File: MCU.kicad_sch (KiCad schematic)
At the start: 23 parts, among them J1 Conn_ARM_SWD_TagConnect_TC203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, U1 MCU_0001, Y1 CLK_0001, Y2 CLK_0002

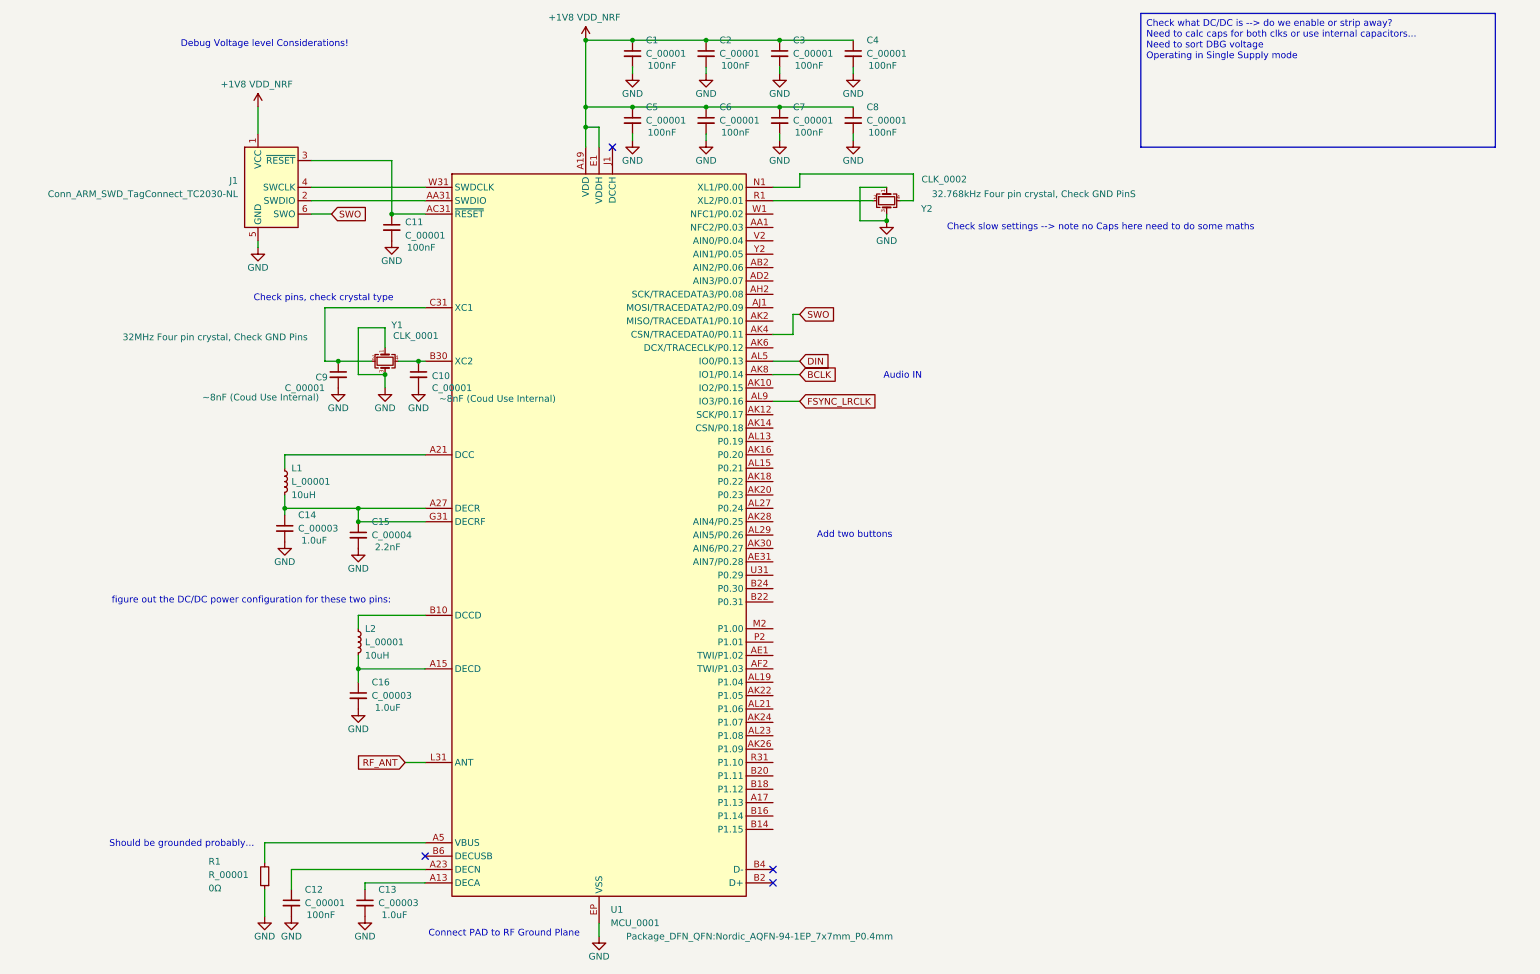
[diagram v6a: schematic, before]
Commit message: added NORA-B106 module, routed SWD/SWO, + power + audio
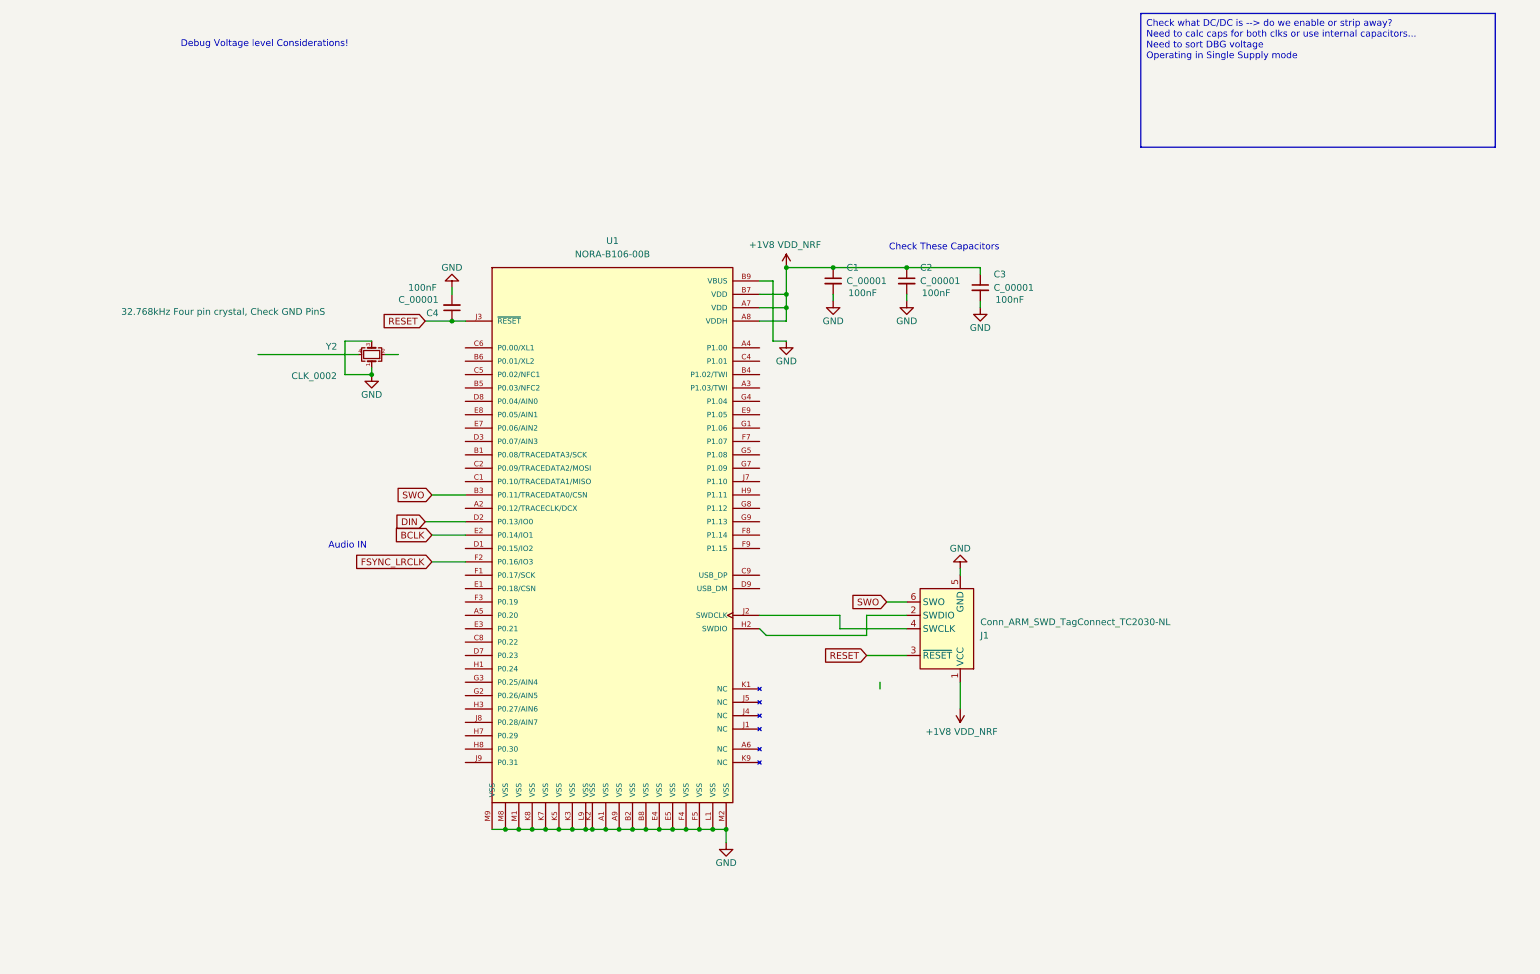
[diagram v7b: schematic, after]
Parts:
- removed C10, C9: C_00001, symbol mic_patch_parts:C_00002
- removed C11, C12, C5, C6, C7, C8: C_00001, symbol mic_patch_parts:C_00001
- removed C13, C14, C16: C_00003, symbol mic_patch_parts:C_00003
- removed C15: C_00004, symbol mic_patch_parts:C_00004
- removed L1, L2: L_00001, symbol mic_patch_parts:L_00001
- removed R1: R_00001, symbol mic_patch_parts:R_00001
- removed U1: MCU_0001, Package_DFN_QFN:Nordic_AQFN-94-1EP_7x7mm_P0.4mm, symbol mic_patch_parts:MCU_0001
- removed Y1: CLK_0001, symbol mic_patch_parts:CLK_0001
- added U1: NORA-B106-00B, NORA-B106-00B:XCVR_NORA-B106-00B, symbol mic_patch_parts:NORA-B106-00B
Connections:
- net +1V8 VDD_NRF: now also U1.A7 (VDD), U1.A8 (VDDH), U1.B7 (VDD); no longer C4.1
- net BCLK: now also U1.E2 (P0.14/IO1)
- net DIN: now also U1.D2 (P0.13/IO0)
- net FSYNC_LRCLK: now also U1.F2 (P0.16/IO3)
- net GND: now also U1.A1 (VSS), U1.A9 (VSS), U1.B2 (VSS), U1.B8 (VSS), U1.B9 (VBUS), U1.E4 (VSS), U1.E5 (VSS), U1.F4 (VSS), U1.F5 (VSS), U1.K2 (VSS), U1.K3 (VSS), U1.K5 (VSS), U1.K7 (VSS), U1.K8 (VSS), U1.L1 (VSS), U1.L9 (VSS), U1.M1 (VSS), U1.M2 (VSS), U1.M8 (VSS), U1.M9 (VSS)
- net SWO: now also U1.B3 (P0.11/TRACEDATA0/CSN)
- net at J1.2 (SWDIO): now also U1.H2 (SWDIO)
- net RESET: now reaches J1.3 (~{RESET})
- net RESET: now also C4.1, U1.J3 (~{RESET})
- net at J1.4 (SWCLK): now also U1.J2 (SWDCLK)
- no-connect marks 4 -> 0
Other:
- note added: "Check These Capacitors"
- note removed: "Add two buttons"
- note removed: "Check pins, check crystal type"
- note removed: "Check slow settings --> note no Caps here need to do some maths"
- note removed: "Connect PAD to RF Ground Plane"
- note removed: "Should be grounded probably..."
- note removed: "figure out the DC/DC power configuration for these two pins:"
- moved on the sheet: C1, C2, J1, Y2

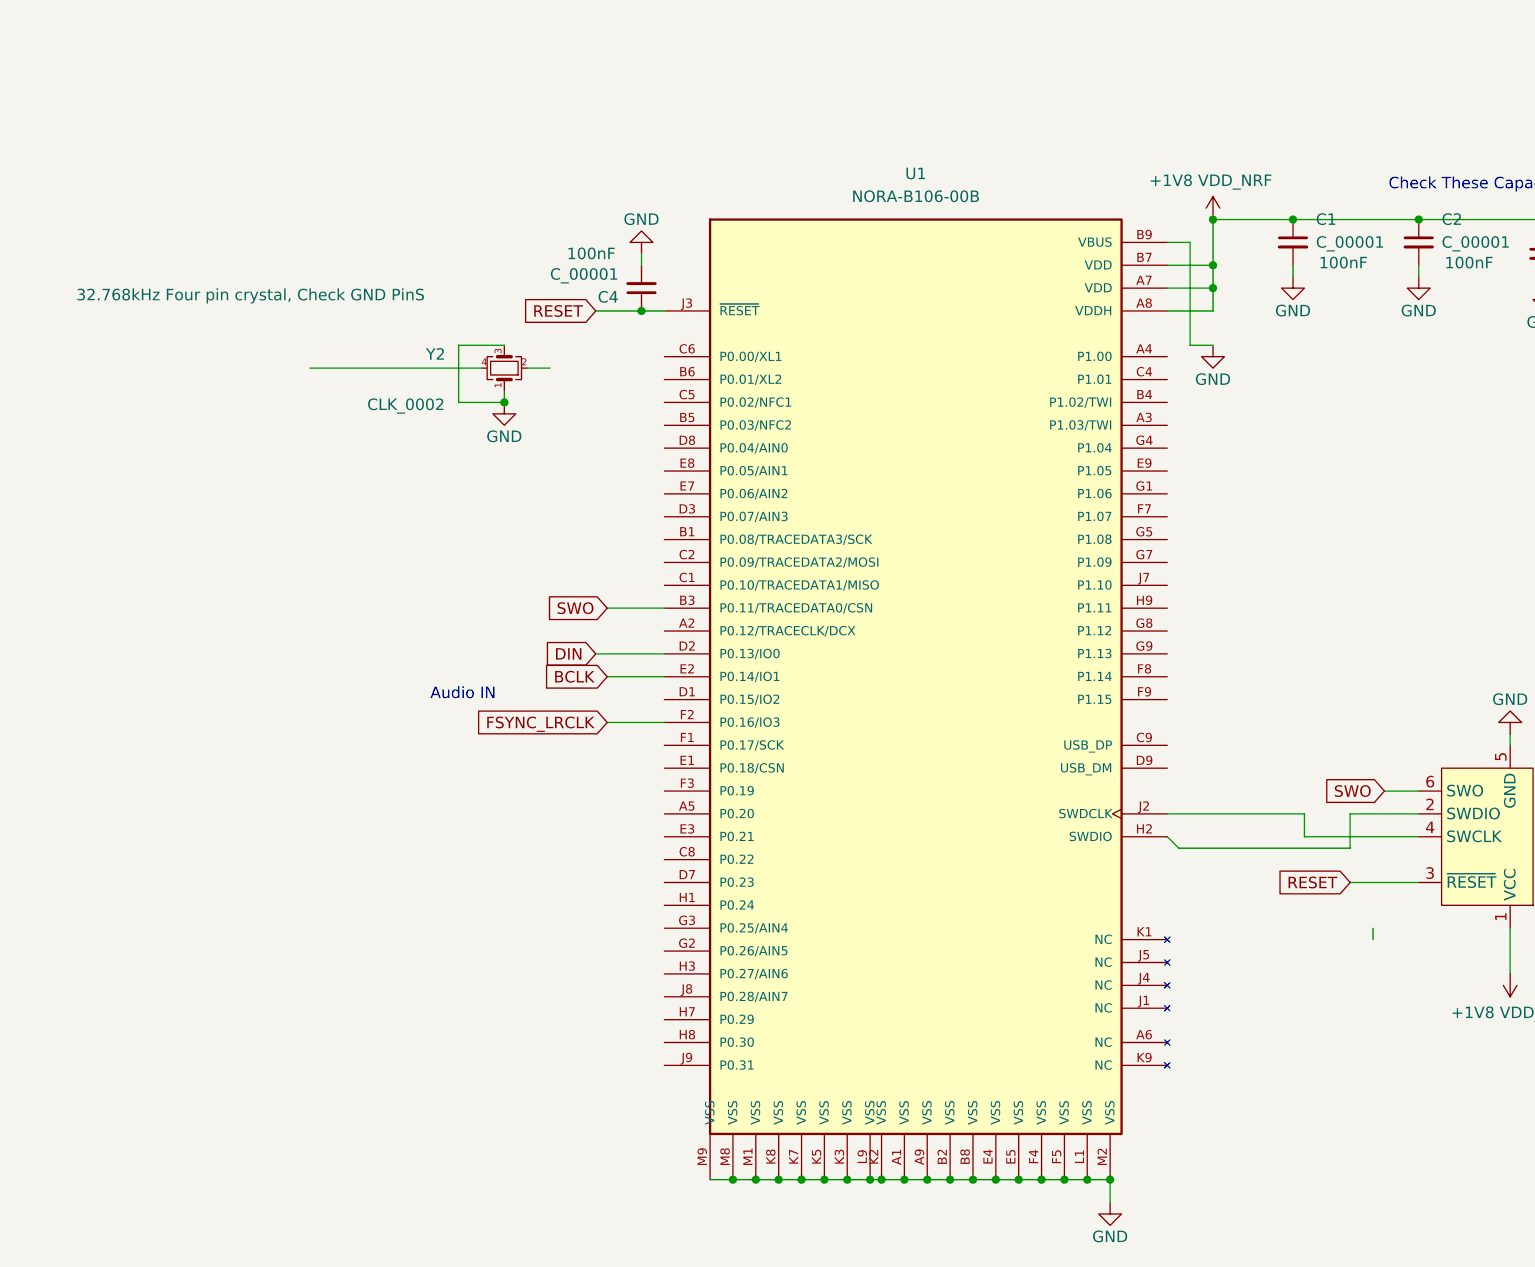
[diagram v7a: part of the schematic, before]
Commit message: updated power supply to 3.0V to support micro SD card
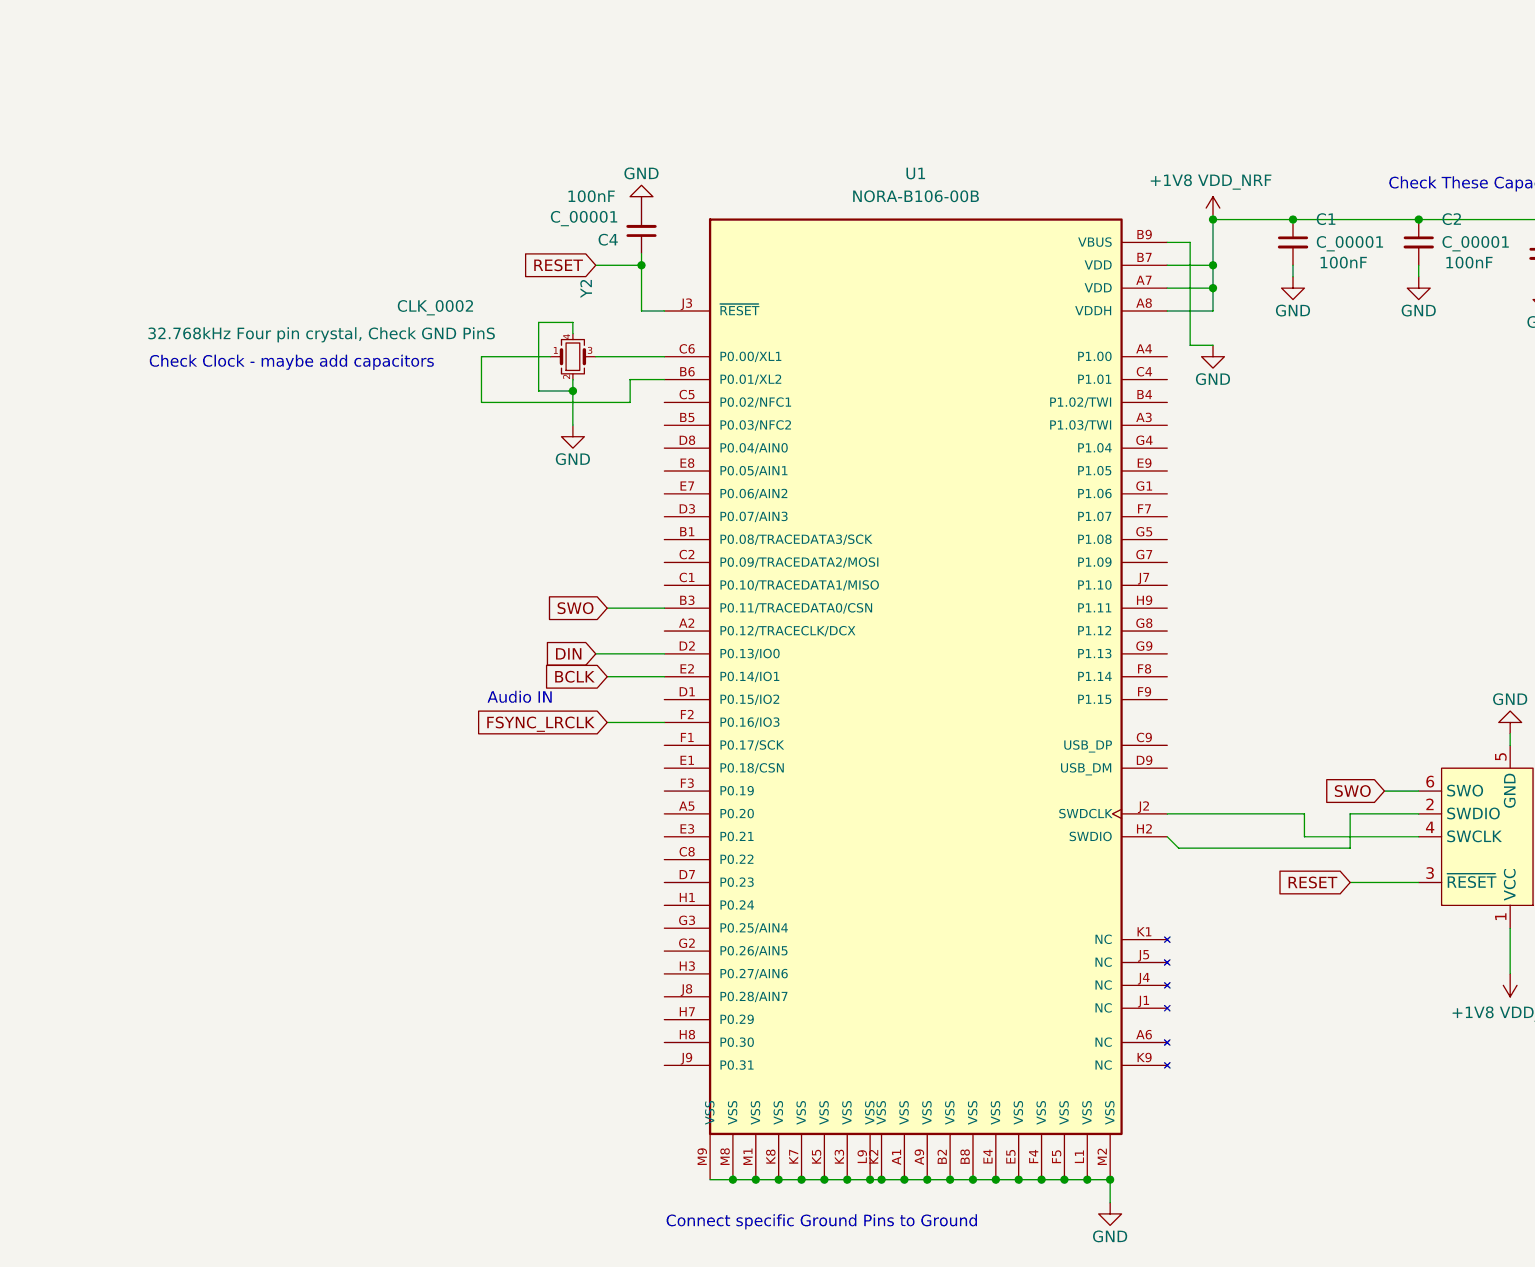
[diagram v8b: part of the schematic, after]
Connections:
- net GND: now also Y2.2, Y2.4; no longer Y2.1, Y2.3
- net at U1.B6 (P0.01/XL2): now also Y2.1
- net at U1.C6 (P0.00/XL1): now also Y2.3
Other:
- note added: "Check Clock - maybe add capacitors"
- note added: "Connect specific Ground Pins to Ground"
- moved on the sheet: C4, Y2
